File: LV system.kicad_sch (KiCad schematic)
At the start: 28 parts, among them K1 SILxx-1Axx-71x, SW1 SW_SPST, SW2 SW_MEC_5G, SW3 SW_SPST

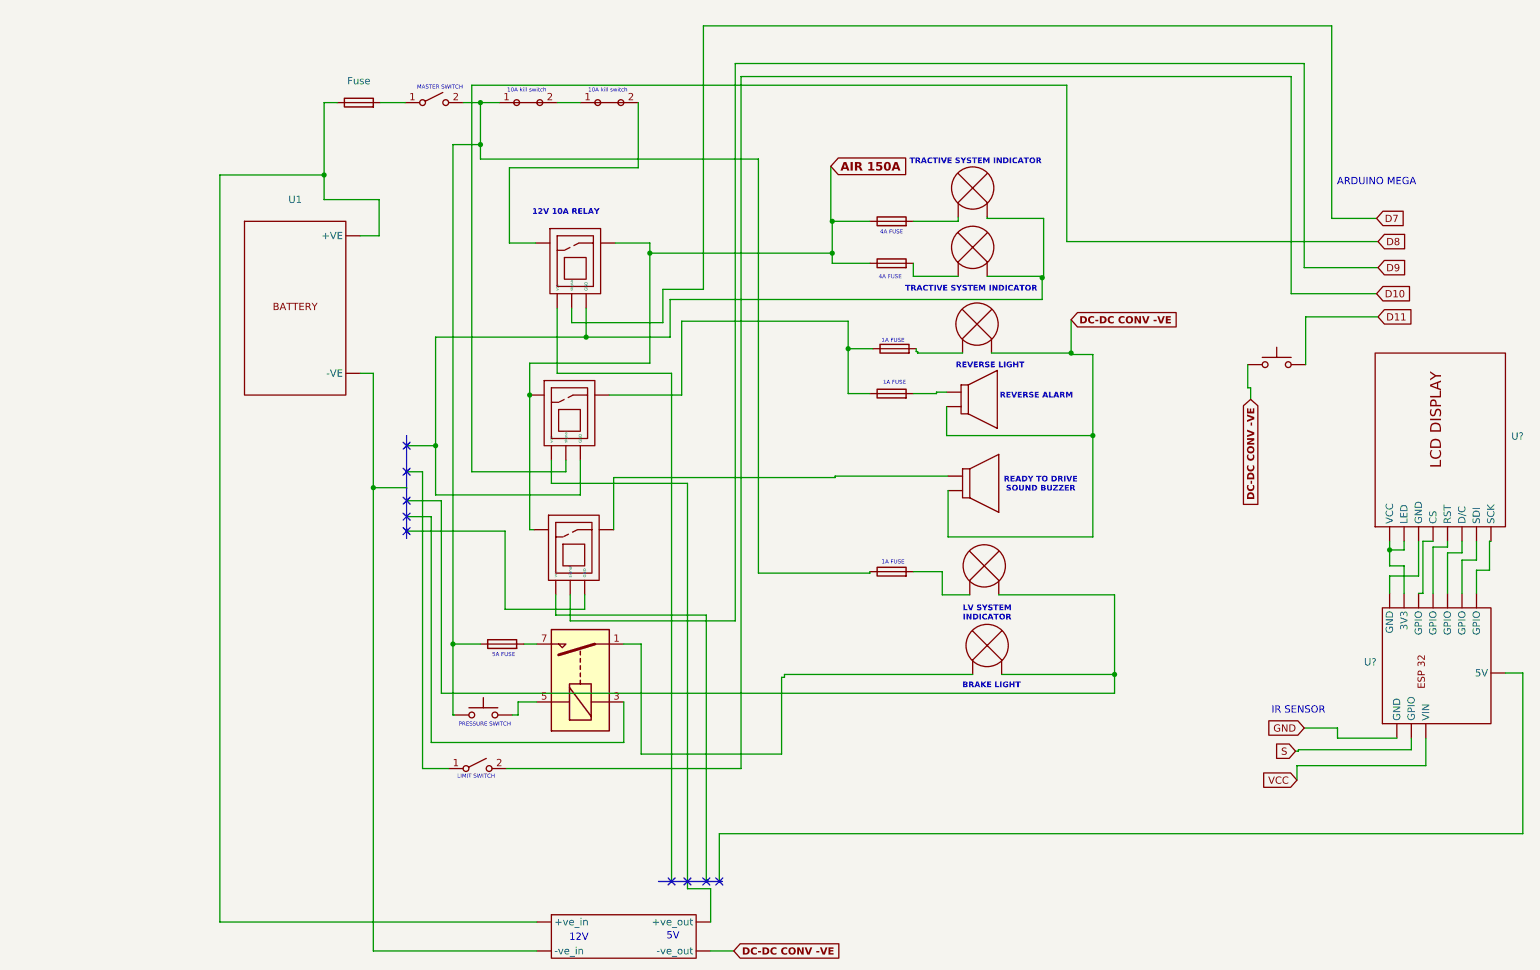
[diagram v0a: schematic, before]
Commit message: Limit switch added
Also colour coded the entire wiring system
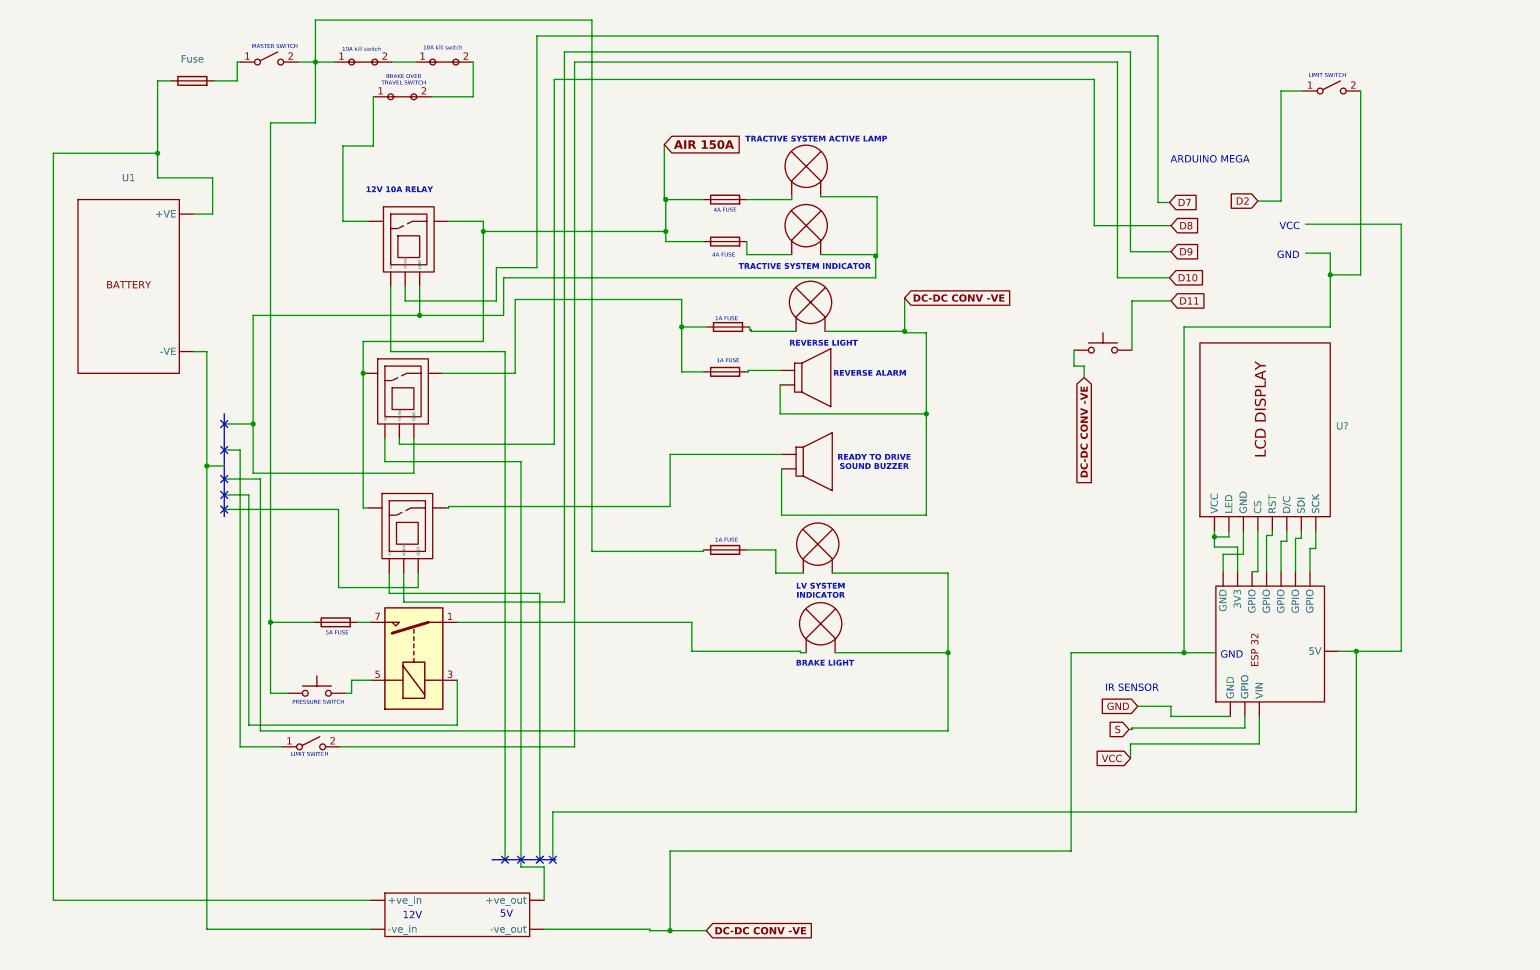
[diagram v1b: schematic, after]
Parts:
- added SW4: SW_SPST, symbol Switch:SW_SPST
- added U15: ~, symbol components:nc_switch
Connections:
- net DC-DC CONV -VE: now also SW4.2 (B)
- net at U9.2: now also U15.2; no longer U6.
- new net: U11., U2., U5., U6.
- new net: U10., U12.
- new net: U?. (GPIO), U?. (SCK) (x6)
- new net: U15.1, U6.
- new net: F1.1, U1. (-VE), U4. (-ve_out)
- new net: U4. (-ve_out), U5.
- new net D2: SW4.1 (A)
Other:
- note added: "BRAKE OVER TRAVEL SWITCH"
- note added: "GND"
- note added: "TRACTIVE SYSTEM ACTIVE LAMP"
- note added: "VCC"
- moved on the sheet: U1, U?

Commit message: AIR Added
Accumulator isolation relay, interlock and fnr is added.
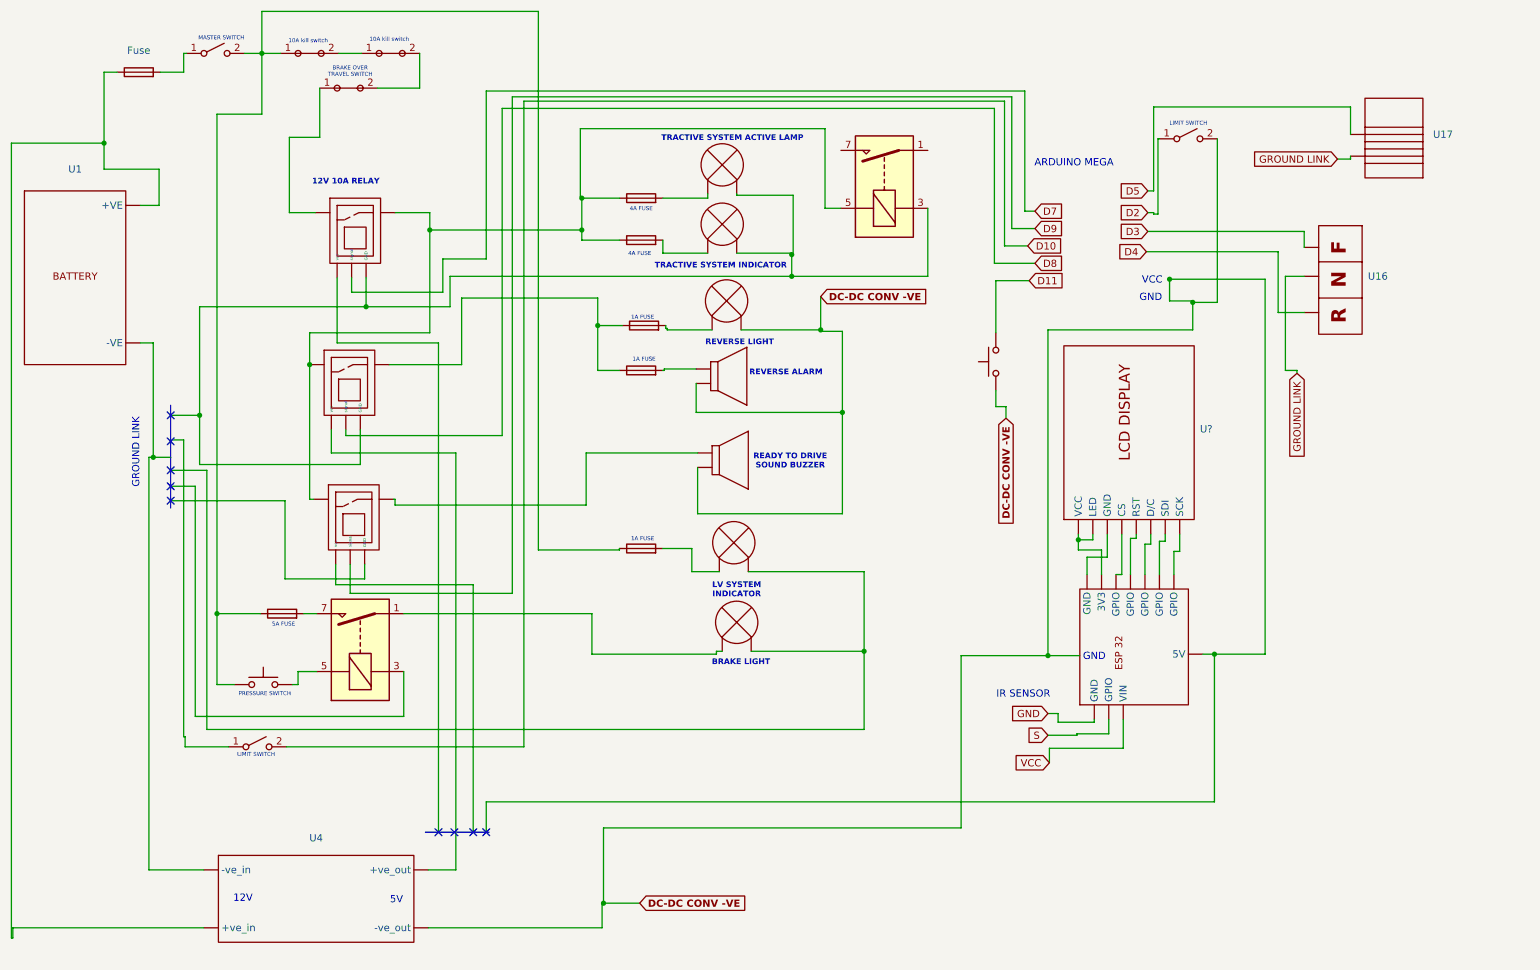
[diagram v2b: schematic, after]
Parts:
- removed U4: ~, symbol LV system components:DC-DC_Conv
- added K2: SILxx-1Axx-71x, Relay_THT:Relay_SPST_StandexMeder_SIL_Form1A, symbol Relay:SILxx-1Axx-71x
- added U16: ~, symbol lv compol:FNR_Switch
- added U17: ~, symbol lv compol:INTERLOCK
- added U4: ~, symbol lv compol:dc_dc_conv
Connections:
- net DC-DC CONV -VE: now also U?. (GPIO), U4. (-ve_out)
- net at F1.1, U1. (-VE): now also U4. (-ve_out)
- removed net AIR 150A: F2.1, F3.1, U10., U5., U6.
- new net: K2.3, U11., U2., U5., U6.
- new net: U10., U12.
- new net: U?. (GPIO), U?. (SCK) (x6)
- new net: U1. (-VE), U4. (-ve_out)
- new net: U4. (-ve_out), U5.
- new net: F2.1, F3.1, K2.5, U10., U5., U6.
- new net D3: U16.
- new net D4: U16.
- new net D5: U17.
- new net GROUND LINK: U16., U17.
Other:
- note added: "GROUND LINK"
- moved on the sheet: U1, U?
